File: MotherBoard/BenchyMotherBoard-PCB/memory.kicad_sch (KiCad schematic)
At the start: 4 parts, among them U19 MT40A1G16TB-062E:F, U4 AM6254ATCGGAALW

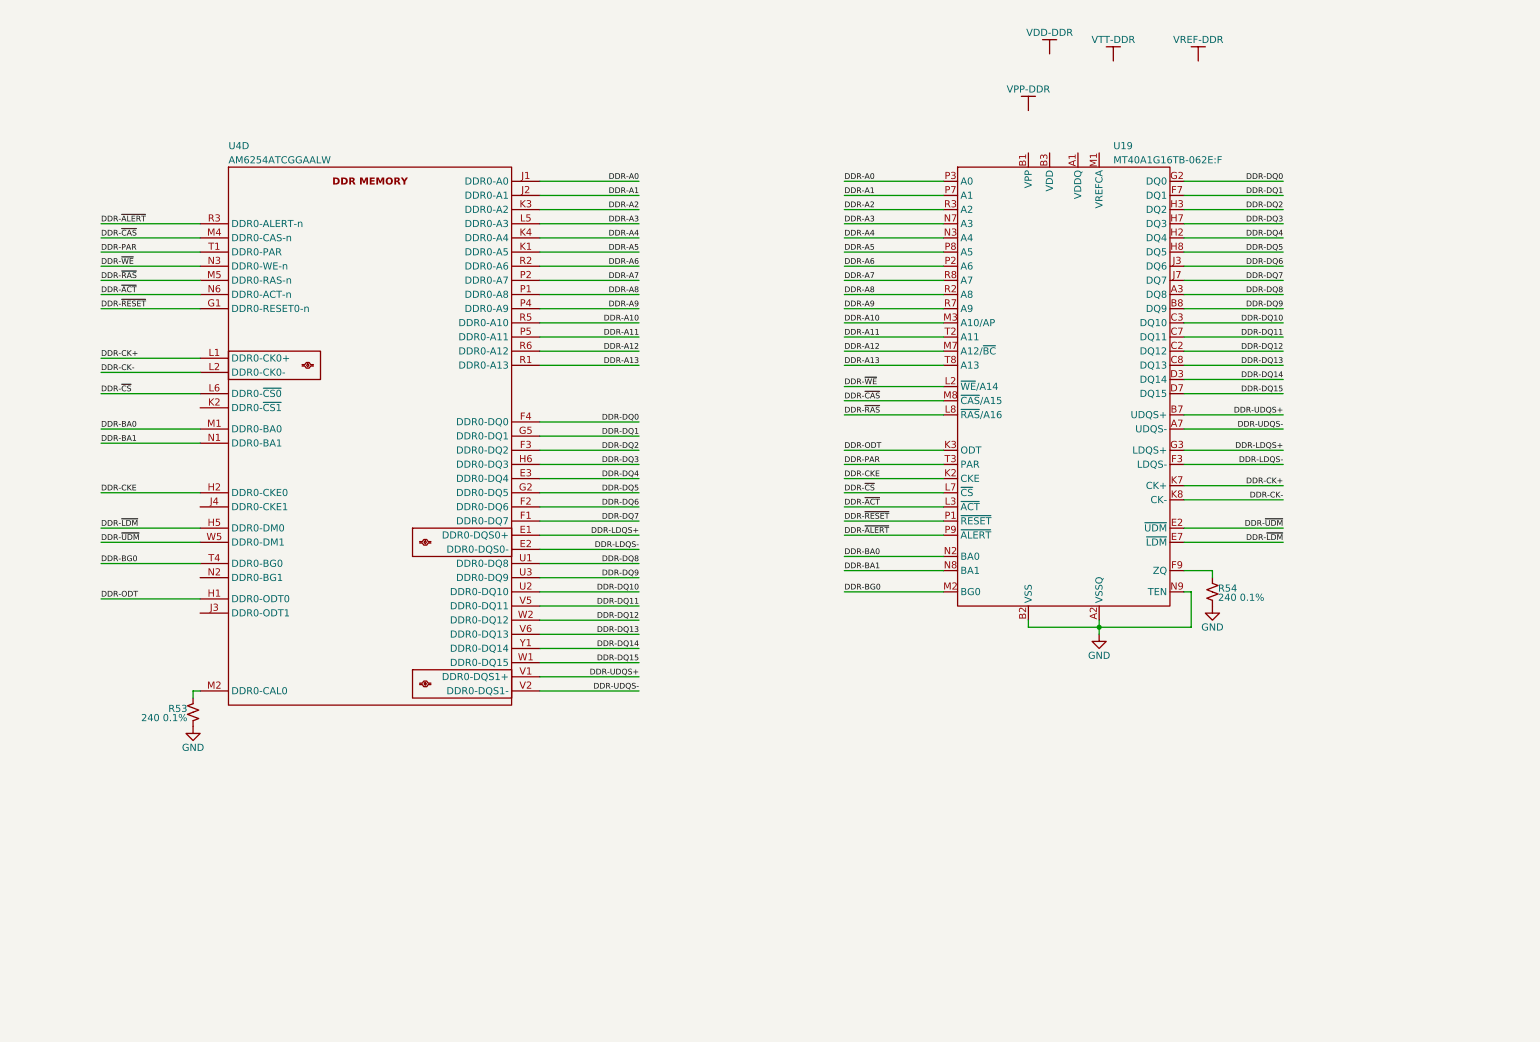
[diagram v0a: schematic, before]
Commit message: (WIP) Complete most of the PS and boot schematics
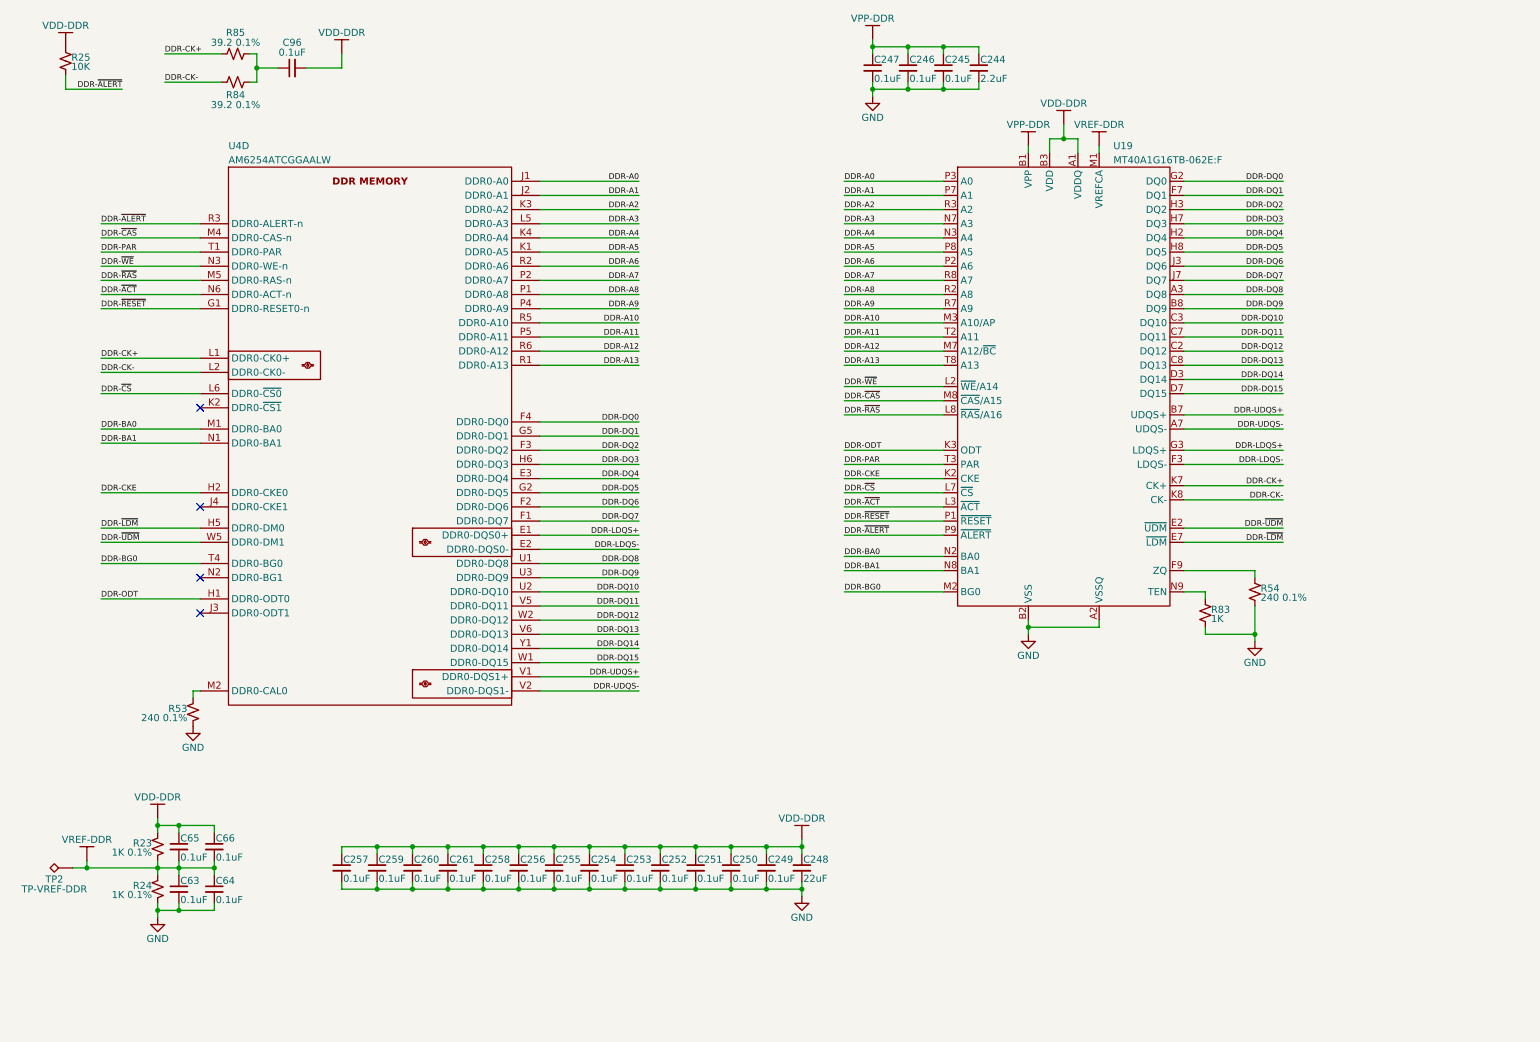
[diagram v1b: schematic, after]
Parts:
- added C244: 2.2uF, Capacitor_SMD:C_0402_1005Metric, symbol Daxxn_Device:C
- added C245, C246, C247, C249, C250, C251, C252, C253, C254, C255, C256, C257, C258, C259, C260, C261, C63, C64, C65, C66, C96: 0.1uF, Capacitor_SMD:C_0201_0603Metric, symbol Daxxn_Device:C
- added C248: 22uF, Capacitor_SMD:C_0805_2012Metric, symbol Daxxn_Device:C
- added R23, R24: 1K 0.1%, Resistor_SMD:R_0201_0603Metric, symbol Daxxn_Device:R
- added R25: 10K, Resistor_SMD:R_0201_0603Metric, symbol Daxxn_Device:R
- added R83: 1K, Resistor_SMD:R_0201_0603Metric, symbol Daxxn_Device:R
- added R84, R85: 39.2 0.1%, Resistor_SMD:R_0201_0603Metric, symbol Daxxn_Device:R
- added TP2: TP-VREF-DDR, TestPoint:TestPoint_Pad_D1.5mm, symbol Connector:TestPoint_Alt
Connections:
- net DDR-CK+: now also R85.1
- net DDR-CK-: now also R84.2
- net DDR-~{ALERT}: now also R25.2
- net GND: now also C244.2, C245.2, C246.2, C247.2, C248.2, C249.2, C250.2, C251.2, C252.2, C253.2, C254.2, C255.2, C256.2, C257.2, C258.2, C259.2, C260.2, C261.2, C63.2, C64.2, R24.2, R83.2; no longer U19.N9 (TEN)
- net VDD-DDR: now also U19.A1 (VDDQ), U19.A9 (VDDQ), U19.B3 (VDD), U19.B9 (VDD), U19.C1 (VDDQ), U19.D1 (VDD), U19.D9 (VDDQ), U19.F2 (VDDQ), U19.F8 (VDDQ), U19.G1 (VDDQ), U19.G7 (VDD), U19.G9 (VDDQ), U19.J1 (VDD), U19.J2 (VDDQ), U19.J8 (VDDQ), U19.J9 (VDD), U19.L1 (VDD), U19.L9 (VDD), U19.R1 (VDD), U19.T9 (VDD), C248.1, C249.1, C250.1, C251.1, C252.1, C253.1, C254.1, C255.1, C256.1, C257.1, C258.1, C259.1, C260.1, C261.1, C65.1, C66.1, C96.2, R23.1, R25.1
- net VPP-DDR: now also U19.B1 (VPP), U19.R9 (VPP), C244.1, C245.1, C246.1, C247.1
- net VREF-DDR: now also U19.M1 (VREFCA), C63.1, C64.1, C65.2, C66.2, R23.2, R24.1, TP2.1
- new net: C96.1, R84.1, R85.2
- new net: R83.1, U19.N9 (TEN)
- no-connect marks 0 -> 4
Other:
- moved on the sheet: R54

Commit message: (WIP) Almost done with schematic
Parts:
- removed U19: MT40A1G16TB-062E:F, Package_BGA:Micron_FBGA-96_7.5x13.5mm_Layout9x16_P0.8mm, symbol Daxxn_Memory:MT40A1G16TB-062E{colon}F
- added C406: 1uF, Capacitor_SMD:C_0402_1005Metric, symbol Daxxn_Device:C
- added C407: 100nF, Capacitor_SMD:C_0402_1005Metric, symbol Daxxn_Device:C
- added C420: 2.2uF, Capacitor_SMD:C_0402_1005Metric, symbol Daxxn_Device:C
- added FB17: 100 @ 100MHz, Inductor_SMD:L_0603_1608Metric, symbol Daxxn_Device:FerriteBead
- added R253, R254, R36: 10K, Resistor_SMD:R_0201_0603Metric, symbol Daxxn_Device:R
- added R28, R29: 2.2K, Resistor_SMD:R_0201_0603Metric, symbol Daxxn_Device:R
- added U19: AS4C512M16D4-75BCN, Package_BGA:Micron_FBGA-96_7.5x13.5mm_Layout9x16_P0.8mm, symbol Daxxn_Memory:AS4C512M16D4-75BCN
- R84, R85: footprint Resistor_SMD:R_0201_0603Metric -> Resistor_SMD:R_0402_1005Metric
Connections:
- net DDR-A0: now also U19.P3 (A0)
- net DDR-A1: now also U19.P7 (A1)
- net DDR-A10: now also U19.M3 (A10/AP)
- net DDR-A11: now also U19.T2 (A11)
- net DDR-A12: now also U19.M7 (A12/~{BC})
- net DDR-A13: now also U19.T8 (A13)
- net DDR-A2: now also U19.R3 (A2)
- net DDR-A3: now also U19.N7 (A3)
- net DDR-A4: now also U19.N3 (A4)
- net DDR-A5: now also U19.P8 (A5)
- net DDR-A6: now also U19.P2 (A6)
- net DDR-A7: now also U19.R8 (A7)
- net DDR-A8: now also U19.R2 (A8)
- net DDR-A9: now also U19.R7 (A9)
- net DDR-BA0: now also U19.N2 (BA0)
- net DDR-BA1: now also U19.N8 (BA1)
- net DDR-BG0: now also U19.M2 (BG0)
- net DDR-CK+: now also U19.K7 (CK+)
- net DDR-CK-: now also U19.K8 (CK-)
- net DDR-CKE: now also R253.2, R254.1, U19.K2 (CKE)
- net DDR-DQ0: now also U19.G2 (DQ0)
- net DDR-DQ1: now also U19.F7 (DQ1)
- net DDR-DQ10: now also U19.C3 (DQ10)
- net DDR-DQ11: now also U19.C7 (DQ11)
- net DDR-DQ12: now also U19.C2 (DQ12)
- net DDR-DQ13: now also U19.C8 (DQ13)
- net DDR-DQ14: now also U19.D3 (DQ14)
- net DDR-DQ15: now also U19.D7 (DQ15)
- net DDR-DQ2: now also U19.H3 (DQ2)
- net DDR-DQ3: now also U19.H7 (DQ3)
- net DDR-DQ4: now also U19.H2 (DQ4)
- net DDR-DQ5: now also U19.H8 (DQ5)
- net DDR-DQ6: now also U19.J3 (DQ6)
- net DDR-DQ7: now also U19.J7 (DQ7)
- net DDR-DQ8: now also U19.A3 (DQ8)
- net DDR-DQ9: now also U19.B8 (DQ9)
- net DDR-LDQS+: now also U19.G3 (LDQS+)
- net DDR-LDQS-: now also U19.F3 (LDQS-)
- net DDR-ODT: now also U19.K3 (ODT)
- net DDR-PAR: now also U19.T3 (PAR)
- net DDR-UDQS+: now also U19.B7 (UDQS+)
- net DDR-UDQS-: now also U19.A7 (UDQS-)
- net DDR-~{ACT}: now also U19.L3 (~{ACT})
- net DDR-~{ALERT}: now also R36.1, U19.P9 (~{ALERT})
- net DDR-~{CAS}: now also U19.M8 (~{CAS}/A15)
- net DDR-~{CS}: now also U19.L7 (~{CS})
- net DDR-~{LDM}: now also U19.E7 (~{LDM})
- net DDR-~{RAS}: now also U19.L8 (~{RAS}/A16)
- net DDR-~{RESET}: now also R28.2, R29.1, U19.P1 (~{RESET})
- net DDR-~{UDM}: now also U19.E2 (~{UDM})
- net DDR-~{WE}: now also U19.L2 (~{WE}/A14)
- net GND: now also C406.2, C407.2, C420.2, R254.2, R29.2, R36.2, U19.A2 (VSSQ), U19.A8 (VSSQ), U19.B2 (VSS), U19.C9 (VSSQ), U19.D2 (VSSQ), U19.D8 (VSSQ), U19.E1 (VSS), U19.E3 (VSSQ), U19.E8 (VSSQ), U19.E9 (VSS), U19.F1 (VSSQ), U19.G8 (VSS), U19.H1 (VSSQ), U19.H9 (VSSQ), U19.K1 (VSS), U19.K9 (VSS), U19.M9 (VSS), U19.N1 (VSS), U19.T1 (VSS)
- net VDD-DDR: now also C420.1, R253.1, R28.1, U19.A1 (VDDQ), U19.A9 (VDDQ), U19.B3 (VDD), U19.B9 (VDD), U19.C1 (VDDQ), U19.D1 (VDD), U19.D9 (VDDQ), U19.F2 (VDDQ), U19.F8 (VDDQ), U19.G1 (VDDQ), U19.G7 (VDD), U19.G9 (VDDQ), U19.J1 (VDD), U19.J2 (VDDQ), U19.J8 (VDDQ), U19.J9 (VDD), U19.L1 (VDD), U19.L9 (VDD), U19.R1 (VDD), U19.T9 (VDD)
- net VPP-DDR: now also C406.1, C407.1, FB17.1; no longer C244.1, C245.1, C246.1, C247.1
- net VREF-DDR: now also U19.M1 (VREFCA)
- net at R54.1: now also U19.F9 (ZQ)
- net at R83.1: now also U19.N9 (TEN)
- new net DDR-VPP: C244.1, C245.1, C246.1, C247.1, FB17.2, U19.B1 (VPP), U19.R9 (VPP)
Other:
- moved on the sheet: C244, C245, C246, C247, C248, C249, C250, C251, C252, C253, C254, C255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

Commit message: Start PCB layout
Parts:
- U23: renamed from U19; footprint Package_BGA:Micron_FBGA-96_7.5x13.5mm_Layout9x16_P0.8mm -> Daxxn_Packages:Micron_FBGA-96_7.5x13.5mm_Layout9x16_P0.8mm
- renumbered C257 to C290, C259 to C291, C260 to C292, C261 to C293, C258 to C294, C256 to C295, C255 to C296, C254 to C297, C253 to C298, C252 to C299, C251 to C300, C250 to C301, C249 to C302, C420 to C303, C248 to C304, C65 to C305, C66 to C306, C247 to C309, C246 to C310, C245 to C311, C244 to C312, C96 to C313, C63 to C314, C64 to C315, R54 to R71, R83 to R72, R53 to R73, R23 to R74, R253 to R75, R28 to R76, R25 to R77, R85 to R78, R84 to R79, R24 to R80, R254 to R81, R29 to R82, R36 to R83

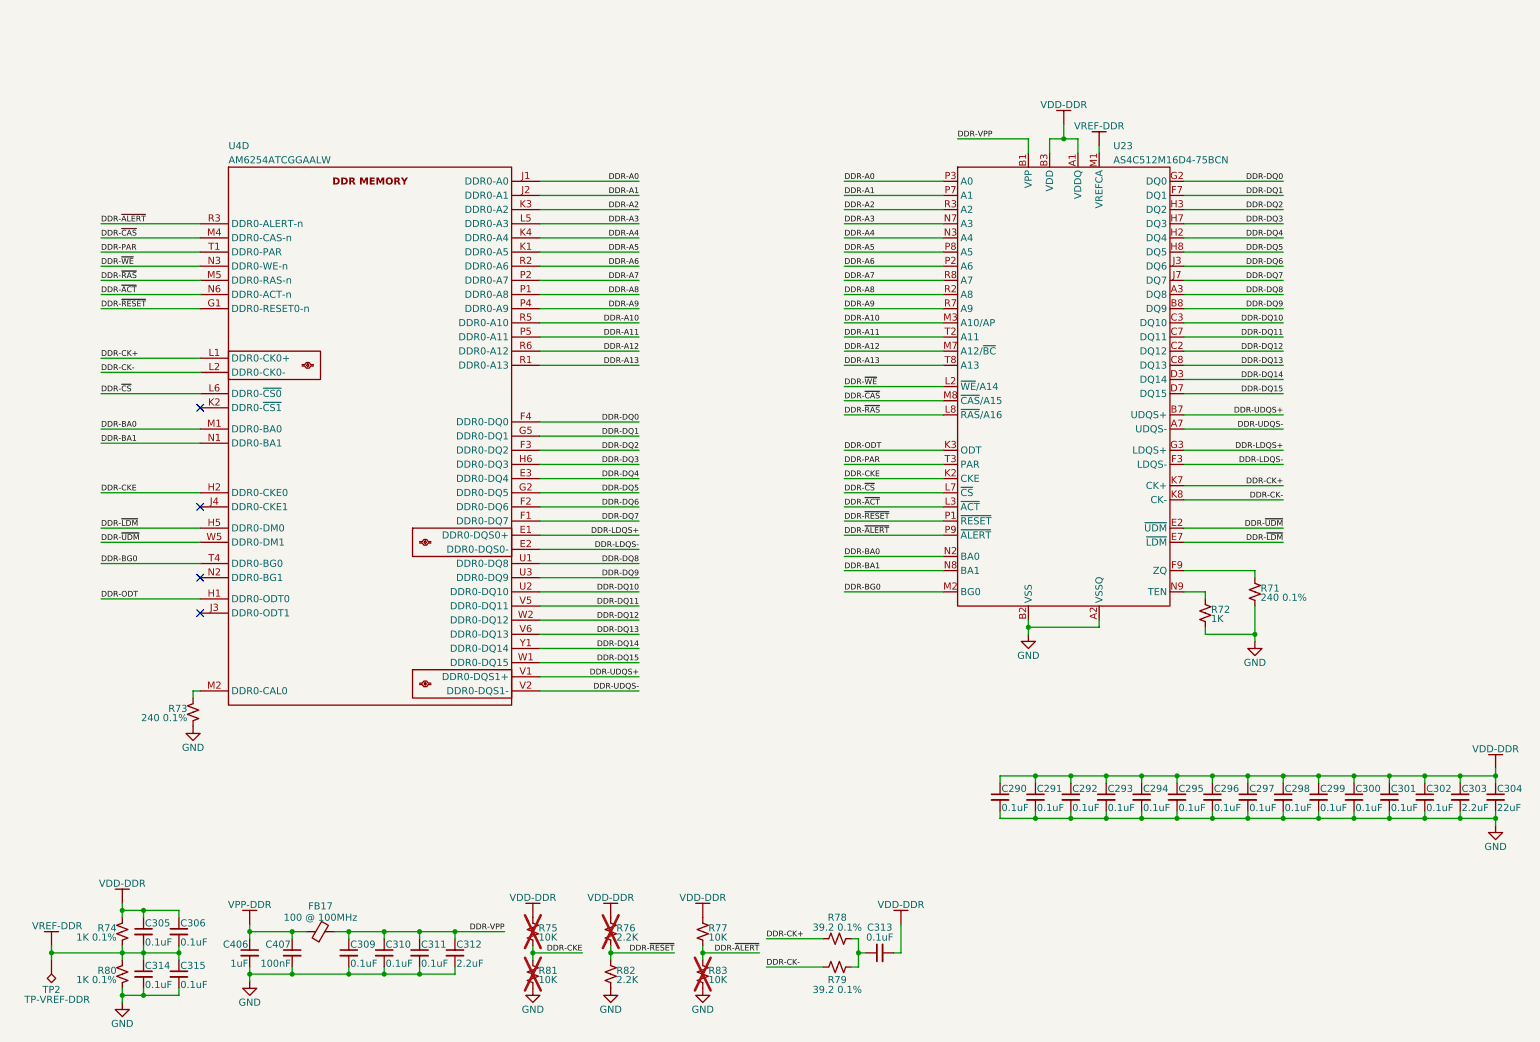
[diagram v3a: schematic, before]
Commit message: Fix power net names and increase PCB size
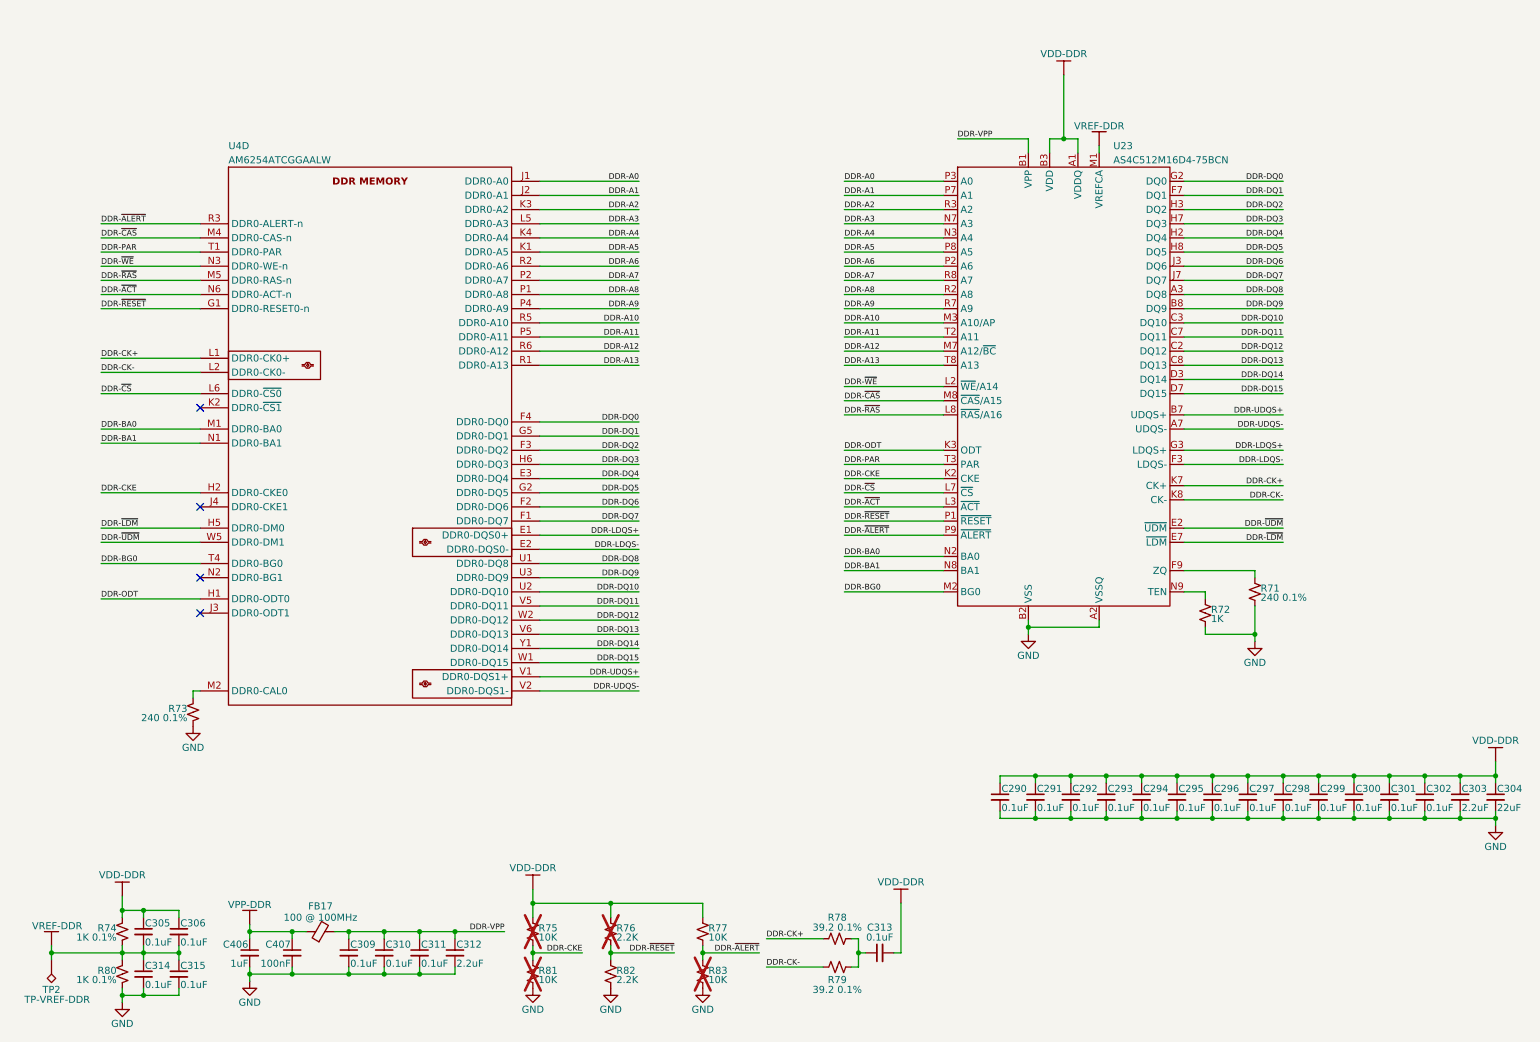
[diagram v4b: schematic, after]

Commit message: (WIP) Still laying out PCB
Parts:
- added C113, C130, C316, C317, C73, C95: 0.1uF, Capacitor_SMD:C_0201_0603Metric, symbol Daxxn_Device:C
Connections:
- net GND: now also C113.2, C130.2, C316.2, C317.2, C73.2, C95.2
- net VDD-DDR: now also C113.1, C130.1, C316.1, C317.1, C73.1, C95.1
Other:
- moved on the sheet: C290, C291, C292, C293, C294, C295, C296, C297, C298, C299, C300, C301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

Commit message: Replacing motherboard and more - SAVE
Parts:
- renumbered C406 to C307, C407 to C308, FB17 to FB19, TP2 to TP13, U4 to U1
